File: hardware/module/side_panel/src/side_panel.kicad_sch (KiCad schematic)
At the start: 50 parts, among them J1 Top Connector, J3 Conn_01x05, J5 Conn_02x07_Odd_Even, M1 GA12-N20 12V 60rpm, Q1 AP2302B, U1 PY32F003F1xPx, U2 L9110S, U3 ITR8307, U4 ITR8307, U5 ITR8307, U6 ITR8307, U7 ITR8307, U8 NUP4202, U9 74LVC1G66

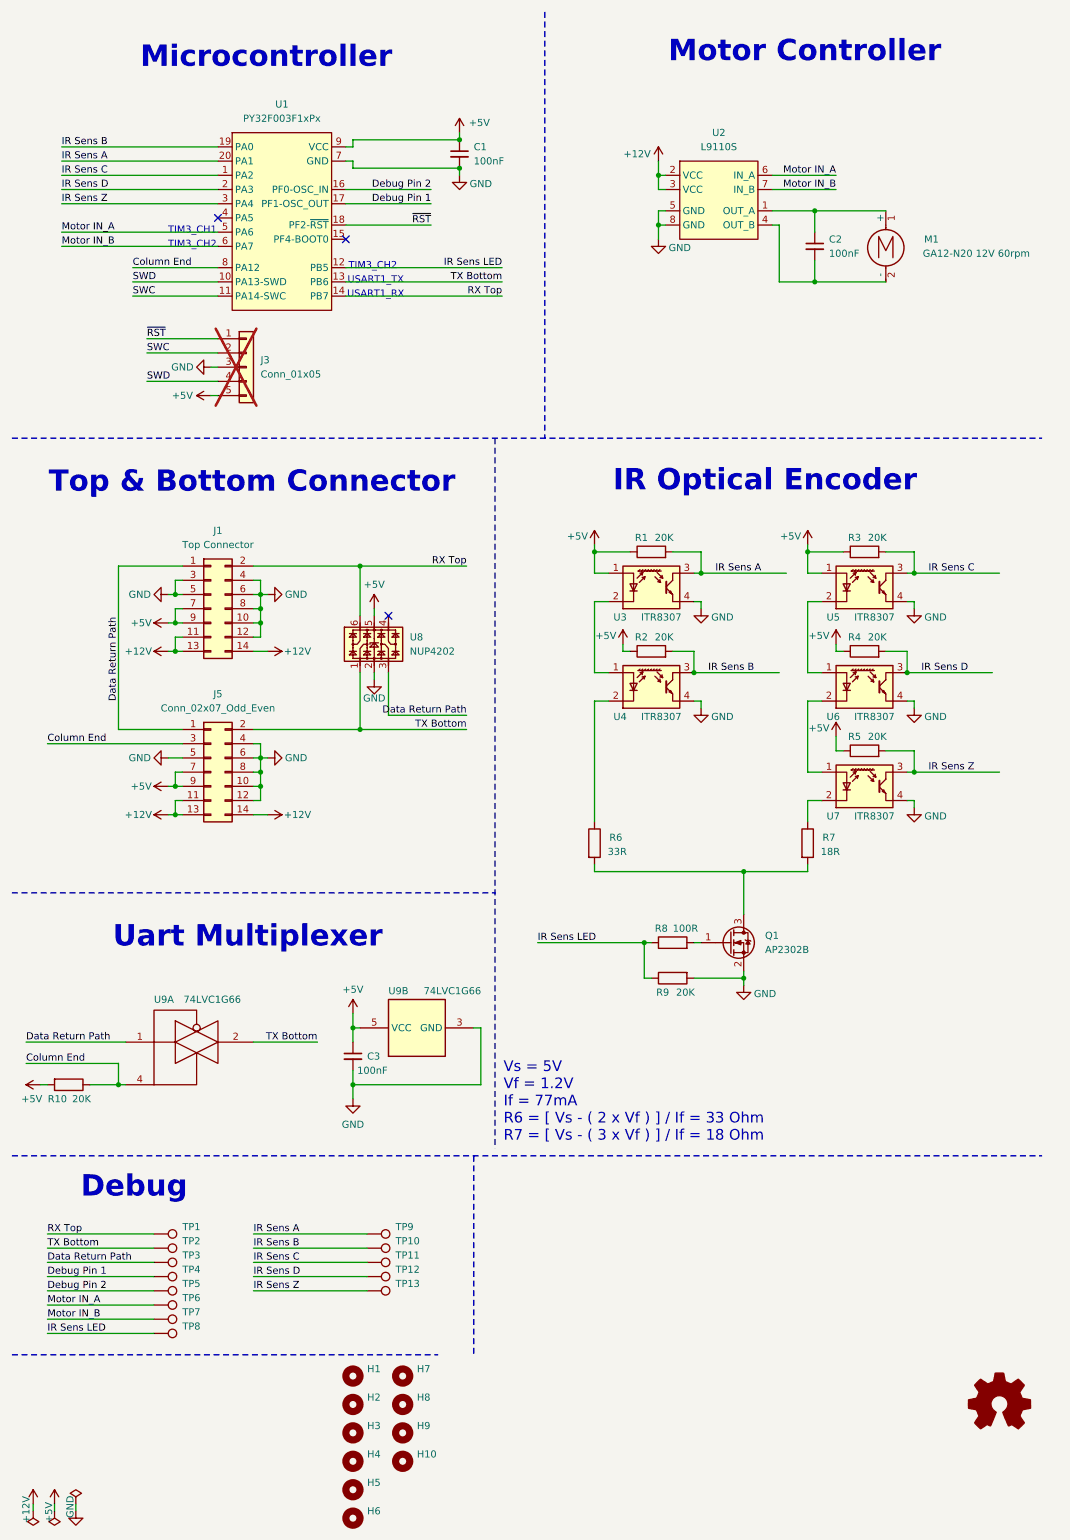
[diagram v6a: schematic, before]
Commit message: Update side panel to add proper ESD protection, 12V detection, removed uart switch in favor of software switching, shuffled around some IO for improved routing.
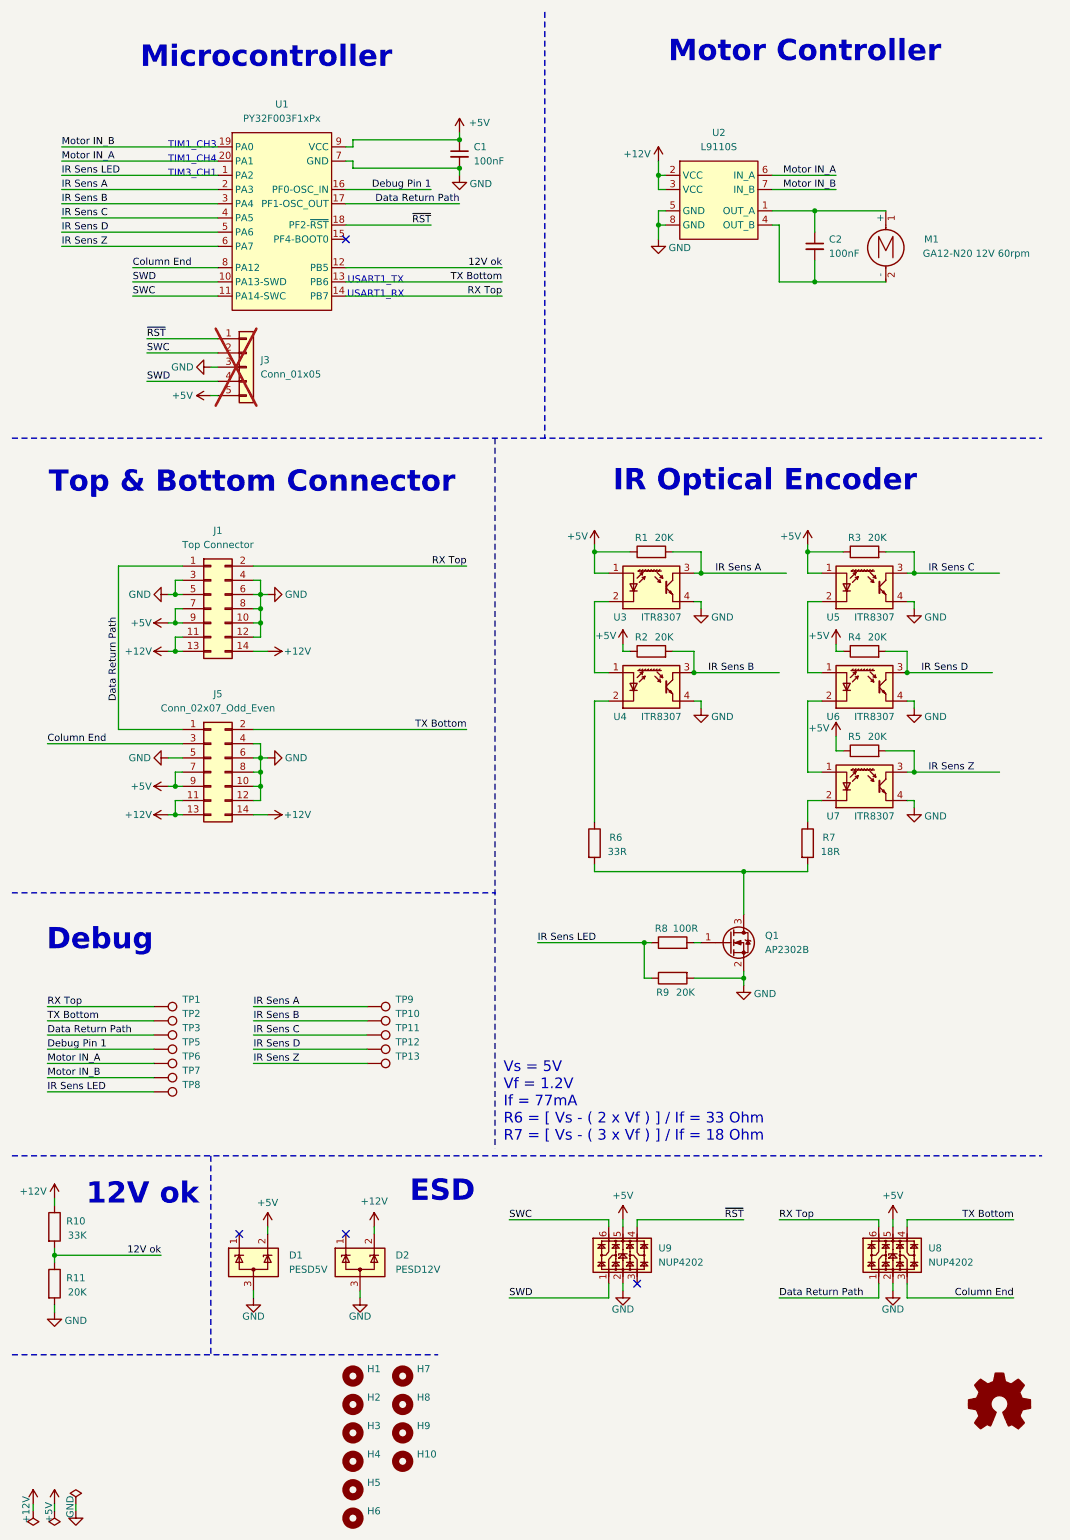
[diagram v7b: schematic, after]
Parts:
- removed C3: 100nF, Capacitor_SMD:C_0805_2012Metric, symbol Device:C_Small
- removed TP4: TestPoint, TestPoint:TestPoint_THTPad_D2.5mm_Drill1.2mm, symbol Connector:TestPoint
- removed U9: 74LVC1G66, Package_TO_SOT_SMD:SOT-23-5, symbol 74xGxx:74LVC1G66
- added D1: PESD5V, Package_TO_SOT_SMD:SOT-23-3, symbol Power_Protection:ESDA5V3L
- added D2: PESD12V, Package_TO_SOT_SMD:SOT-23-3, symbol Power_Protection:ESDA5V3L
- added R11: 20K, Resistor_SMD:R_0805_2012Metric, symbol Device:R
- added U9: NUP4202, Package_TO_SOT_SMD:SOT-23-6, symbol Power_Protection:NUP4202
- R10: value 20K -> 33K
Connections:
- net Debug Pin 2 is gone; now on net Debug Pin 1: TP5.1, U1.16 (PF0-OSC_IN)
- net +12V: now also R10.1, D2.2 (K)
- net +5V: now also D1.2 (K), U9.5; no longer R10.2
- net Column End: now also U8.3; no longer R10.1
- net Data Return Path: now also U1.17 (PF1-OSC_OUT), U8.1; no longer U8.3
- net Debug Pin 1: no longer U1.17 (PF1-OSC_OUT)
- net GND: now also D1.3 (A), D2.3 (A), R11.2, U9.2
- net IR Sens A: now also U1.2 (PA3); no longer U1.20 (PA1)
- net IR Sens B: now also U1.3 (PA4); no longer U1.19 (PA0)
- net IR Sens C: now also U1.4 (PA5); no longer U1.1 (PA2)
- net IR Sens D: now also U1.5 (PA6); no longer U1.2 (PA3)
- net IR Sens LED: now also U1.1 (PA2); no longer U1.12 (PB5)
- net IR Sens Z: now also U1.6 (PA7); no longer U1.3 (PA4)
- net Motor IN_A: now also U1.20 (PA1); no longer U1.5 (PA6)
- net Motor IN_B: now also U1.19 (PA0); no longer U1.6 (PA7)
- net SWC: now also U9.6
- net SWD: now also U9.1
- net TX Bottom: now also U8.4; no longer U8.1
- net ~{RST}: now also U9.4
- new net 12V ok: R10.2, R11.1, U1.12 (PB5)
- no-connect marks 3 -> 4
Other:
- note added: "12V ok"
- note added: "ESD"
- note added: "TIM1_CH3"
- note added: "TIM1_CH4"
- note removed: "TIM3_CH2"
- note removed: "Uart Multiplexer"
- moved on the sheet: TP1, TP10, TP11, TP12, TP13, TP2, TP3, TP5, TP6, TP7, TP8, TP9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

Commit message: side panel v7
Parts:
- removed R1, R2: 20K, Resistor_SMD:R_0805_2012Metric, symbol Device:R
- removed R6: 33R, Resistor_SMD:R_0805_2012Metric, symbol Device:R
- removed TP11: TestPoint, TestPoint:TestPoint_THTPad_D2.5mm_Drill1.2mm, symbol Connector:TestPoint
- removed U3, U4: ITR8307, OptoDevice:OnSemi_CASE100CY, symbol Sensor_Proximity:QRE1113GR
- added TP13, TP4: TestPoint, TestPoint:TestPoint_THTPad_D2.5mm_Drill1.2mm, symbol Connector:TestPoint
- renumbered R3 to R1, R4 to R2, R5 to R3, R7 to R4, R8 to R5, R9 to R6, R10 to R7, R11 to R8, TP13 to TP11, U5 to U3, U6 to U4, U7 to U5
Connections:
- net IR Sens C is gone; now on net IR Sens A: R1.2, U1.4 (PA5), U3.3
- net Data Return Path: now also U1.1 (PA2); no longer U1.17 (PF1-OSC_OUT)
- net IR Sens A: no longer U1.2 (PA3)
- net IR Sens B: now also R2.2, U1.5 (PA6), U4.3; no longer U1.3 (PA4)
- net IR Sens LED: now also U1.3 (PA4); no longer U1.1 (PA2)
- net RX Top: now also U1.2 (PA3); no longer U1.14 (PB7)
- net TX Bottom: now also U1.17 (PF1-OSC_OUT); no longer U1.13 (PB6)
- net Debug Pin 2: now reaches U1.15 (PF4-BOOT0)
- net Debug Pin 2: now also TP4.1
- removed net IR Sens D: R2.2, TP12.1, U1.5 (PA6), U4.3
- new net Debug Pin 3: TP12.1, U1.13 (PB6)
- new net Debug Pin 4: TP13.1, U1.14 (PB7)
- no-connect marks 4 -> 3
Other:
- note added: "TIM3_CH2"
- note added: "TIM3_CH3"
- note added: "Vs = 5V Vf = 1.2V If = 77mA R4 = [ Vs - ( 3 x Vf ) ] / If = 18 Ohm"
- note removed: "Vs = 5V Vf = 1.2V If = 77mA R6 = [ Vs - ( 2 x Vf ) ] / If = 33 Ohm R7 = [ Vs - ( 3 x Vf ) ] / If = 18 Ohm"
- moved on the sheet: R1, R2, R3, R4, TP10, TP11, TP9, U3, U4, U5
